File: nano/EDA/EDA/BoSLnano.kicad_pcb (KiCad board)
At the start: 4 copper layers, 69.2 x 15 mm, 60 parts, among them J1 Micro_SD_Card, J2 Conn_01x07, J3 Conn_01x04, J4 SAMD_DBG, J5 nRF_DBG, J6 Conn_01x10, J7 Conn_01x04, J8 Jack-DC, J9 USB_B_Micro, SW1 SPST, U1 MCP1700-3302E_SOT23, U2 ATSAMD21G18A-MUT, U3 NT3H2111W0FTT, U4 NRF9160, U5 BGA524N6, U6 MSQA6V1W5T2G, U7 MAX40203ANS, U8 MAX40203ANS, Y1 32.768kHz

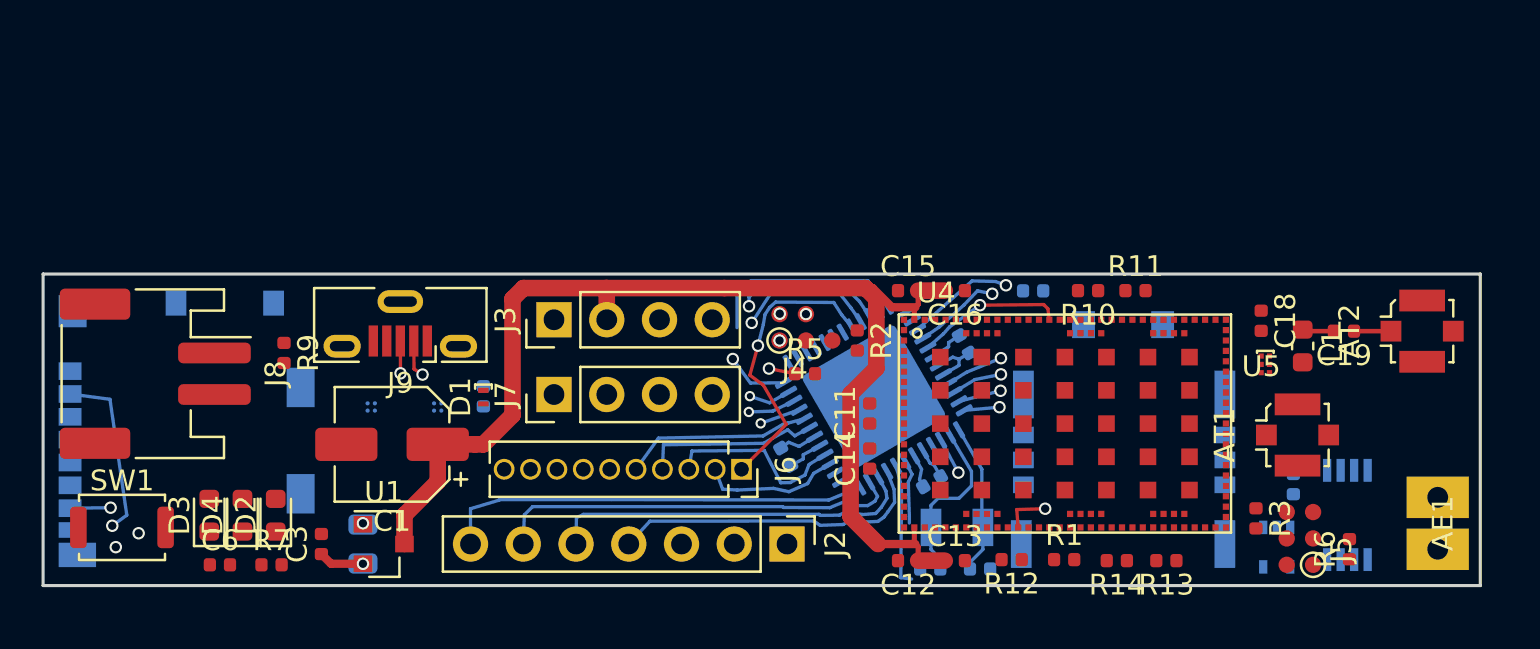
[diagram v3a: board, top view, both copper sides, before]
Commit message: made to be 70 mm
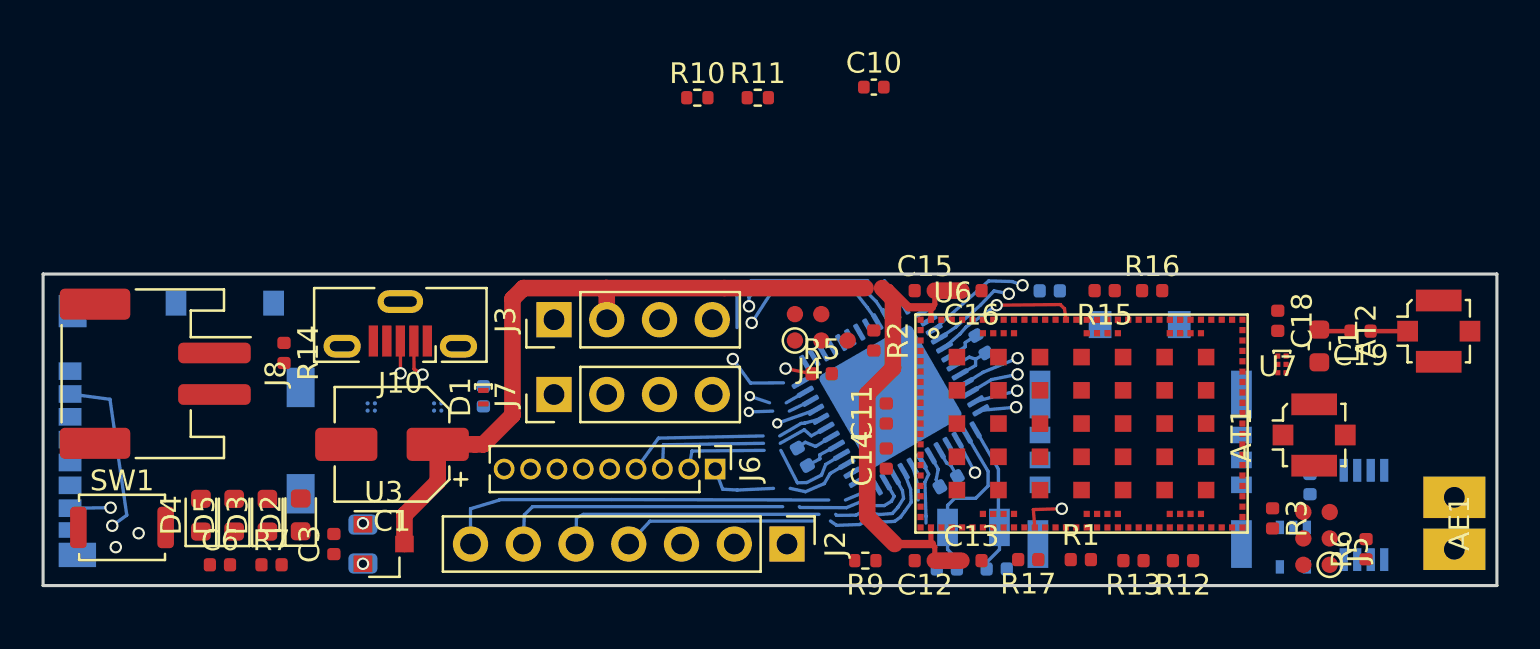
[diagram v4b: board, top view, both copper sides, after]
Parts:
- removed I1: SIM, SIMFootprints:SIMNano
- removed the R14 at (151.7, 113.8)
- removed the U2 at (140.0, 105.9)
- removed the U3 at (162.8, 111.6)
- added C8: 1 μF, Capacitor_SMD:C_0402_1005Metric, B.Cu at (145.2, 103.4)
- added D2: LED, LED_SMD:LED_0603_1608Metric, F.Cu at (112.4, 111.6)
- added J9: SIM, SIMFootprints:SIMNano, B.Cu at (152.8, 114.5)
- added R15: 3.3 kΩ, Resistor_SMD:R_0402_1005Metric, F.Cu at (151.1, 100.8)
- added R16: 3.3 kΩ, Resistor_SMD:R_0402_1005Metric, F.Cu at (153.4, 100.8)
- added R17: 10 kΩ, Resistor_SMD:R_0402_1005Metric, F.Cu at (147.4, 113.8)
- added R9: 3.3 kΩ, Resistor_SMD:R_0402_1005Metric, F.Cu at (139.6, 113.8)
- added U7: BGA524N6, SIMFootprints:TSNP-6-2, F.Cu at (159.4, 104.0)
- added U8: MSQA6V1W5T2G, Package_TO_SOT_SMD:SOT-353_SC-70-5, B.Cu at (160.2, 113.2)
- C10: moved to F.Cu
- C9: value 1 μF -> 100 nF
- J6: value Conn_01x10 -> Conn_01x09; footprint Connector_PinSocket_1.27mm:PinSocket_1x10_P1.27mm_Vertical -> Connector_PinHeader_1.27mm:PinHeader_1x09_P1.27mm_Vertical
- R10: value 3.3 kΩ -> 12 MΩ
- R11: value 3.3 kΩ -> 3.3 MΩ
- R13: value 10 kΩ -> 18 kΩ
- U4: value NRF9160 -> ATSAMD21G18A-MUT; footprint SIMFootprints:nRF9160 -> Package_DFN_QFN:QFN-48-1EP_7x7mm_P0.5mm_EP5.15x5.15mm; moved to B.Cu
- U5: value BGA524N6 -> NT3H2111W0FTT; footprint SIMFootprints:TSNP-6-2 -> Package_SO:TSSOP-8_3x3mm_P0.65mm; moved to B.Cu
- U6: value MSQA6V1W5T2G -> NRF9160; footprint Package_TO_SOT_SMD:SOT-353_SC-70-5 -> SIMFootprints:nRF9160; moved to F.Cu
- moved R10 21.0 mm to (131.5, 91.5), turned to 0 degrees
- moved R11 20.4 mm to (134.4, 91.5)
- moved C10 19.2 mm to (140.0, 91.0), turned to 0 degrees
- moved U6 11.1 mm to (150.0, 107.2), turned to 0 degrees
- moved U5 9.11 mm to (163.6, 111.6), turned to 90 degrees
- moved U4 8.50 mm to (140.8, 105.9), turned to 120 degrees
- moved R12 8.25 mm to (154.9, 113.8)
- moved C9 6.66 mm to (143.6, 110.0), turned to 210 degrees
- moved R13 1.59 mm to (152.5, 113.8)
- moved J6 1.27 mm to (132.4, 109.4)
- moved C17 0.80 mm to (148.5, 100.8)
- moved C19 0.80 mm to (163.4, 102.8)
- moved C7 0.80 mm to (136.6, 108.8)
- moved J5 0.80 mm to (161.3, 115.3)
- moved R1 0.80 mm to (150.0, 113.8)
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- renumbered D2 to D3, D3 to D4, D4 to D5, J9 to J10, R9 to R14, U7 to U1, U8 to U2, U1 to U3
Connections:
- C10 pad 1: -BATT -> Net-(C10-Pad1)
- C10 pad 2: V_3.3 -> -BATT
- C9 pad 1: V_3.3 -> -BATT
- C9 pad 2: -BATT -> V_3.3
- D4 pad 2: Net-(D3-Pad2) (its old number) -> Net-(D4-Pad2)
- D5 pad 2: Net-(D4-Pad2) -> Net-(D5-Pad2)
- J6 pad 1: D1 -> D2
- J6 pad 2: D2 -> D3
- J6 pad 3: D3 -> D4
- J6 pad 4: D4 -> D5
- J6 pad 5: D5 -> D6
- J6 pad 6: D6 -> D7
- J6 pad 7: D7 -> D8
- J6 pad 8: D8 -> D9
- J6 pad 9: D9 -> D10
- R10 pad 1: nRF_STAT -> Net-(C10-Pad1)
- R10 pad 2: Net-(D3-Pad2) (its old number) -> -BATT
- R11 pad 1: nRF_PWR -> Net-(C10-Pad1)
- R11 pad 2: Net-(D4-Pad2) -> +BATT
- R12 pad 1: nRF_RST -> USB_V
- R12 pad 2: V_3.3 -> Net-(R12-Pad2)
- R13 pad 1: USB_V -> Net-(R12-Pad2)
- R13 pad 2: Net-(R13-Pad2) -> -BATT
- U4 pad 1: -BATT -> Net-(C4-Pad1)
- U4 pad 10: Net-(U4-Pad10) -> A4
- U4 pad 11: -BATT -> A5
- U4 pad 12: V_3.3 -> A6
- U4 pad 13: Net-(C14-Pad2) -> SDA
- U4 pad 14: -BATT -> SCL
- U4 pad 15: Net-(U4-Pad15) -> D2
- U4 pad 16: Net-(U4-Pad16) -> D3
- U4 pad 17: -BATT -> V_3.3
- U4 pad 18: RX -> -BATT
- U4 pad 19: TX -> D4
- U4 pad 2: Net-(U4-Pad2) -> Net-(C5-Pad2)
- U4 pad 20: Net-(U4-Pad20) -> D5
- U4 pad 21: -BATT -> SD_MOSI
- U4 pad 22: VPP -> SD_SCLK
- U4 pad 23: Net-(U4-Pad23) -> SD_CS
- U4 pad 24: Net-(U4-Pad24) -> SD_MISO
- U4 pad 25: Net-(U4-Pad25) -> D8
- U4 pad 26: Net-(U4-Pad26) -> D9
- U4 pad 27: -BATT -> Net-(D1-Pad2)
- U4 pad 28: Net-(U4-Pad28) -> D10
- U4 pad 29: Net-(U4-Pad29) -> D6
- U4 pad 3: Net-(U4-Pad3) -> A0
- U4 pad 30: Net-(U4-Pad30) -> D7
- U4 pad 31: -BATT -> NFC_I
- U4 pad 32: nRF_RST -> nRF_EN
- U4 pad 33: nRF_SWCLK -> USB_DM
- U4 pad 34: nRF_SWDIO -> USB_DP
- U4 pad 35: Net-(U4-Pad35) -> -BATT
- U4 pad 36: -BATT -> V_3.3
- U4 pad 37: Net-(U4-Pad37) -> TX
- U4 pad 38: Net-(U4-Pad38) -> RX
- U4 pad 39: Net-(U4-Pad39) -> nRF_RST
- U4 pad 4: Net-(U4-Pad4) -> VNFC
- U4 pad 40: Net-(U4-Pad40) -> RST
- U4 pad 41: -BATT -> nRF_SW_EN
- U4 pad 42: Net-(R13-Pad2) -> -BATT
- U4 pad 43: Net-(I1-Pad2) -> V_3.3
- U4 pad 44: -BATT -> V_3.3
- U4 pad 45: Net-(U4-Pad45) -> SWCLK
- U4 pad 46: Net-(I1-Pad3) -> SWDIO
- U4 pad 47: -BATT -> A1
- U4 pad 48: Net-(I1-Pad6) -> A2
- U4 pad 49: Net-(C17-Pad2) -> (no net)
- U4 pad 6: -BATT -> V_3.3
- U4 pad 7: -BATT -> Net-(R9-Pad1)
- U4 pad 8: -BATT -> Net-(C10-Pad1)
- U4 pad 9: -BATT -> A3
- U5 pad 1: -BATT -> Net-(AE1-Pad2)
- U5 pad 2: V_3.3 -> -BATT
- U5 pad 3: Net-(U4-Pad67) -> SCL
- U5 pad 4: -BATT -> NFC_I
- U5 pad 5: Net-(L1-Pad2) -> SDA
- U5 pad 6: Net-(U4-Pad93) -> VNFC
- U6 pad 1: Net-(I1-Pad2) -> -BATT
- U6 pad 2: -BATT -> Net-(U6-Pad2)
- U6 pad 3: Net-(I1-Pad3) -> Net-(U6-Pad3)
- U6 pad 4: Net-(I1-Pad6) -> Net-(U6-Pad4)
- U6 pad 5: Net-(C17-Pad2) -> -BATT
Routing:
- net D1: track 14.1 -> 0.00 mm, vias 1 -> 0
- net nRF_EN: track 5.93 -> 0.00 mm
- net VNFC: track 3.11 -> 0.00 mm
- net Net-(R9-Pad1): track 0.00 -> 3.11 mm
- net V_3.3: track 18.5 -> 16.3 mm, vias 2 -> 1
- net Net-(C10-Pad1): track 0.00 -> 1.66 mm
- net SWCLK: vias 2 -> 1
- net SWDIO: vias 2 -> 1
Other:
- board size 69.2 x 15 mm -> 70 x 15 mm
- board text added: "BoSLnano rev 0.1.0"

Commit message: began routing nano
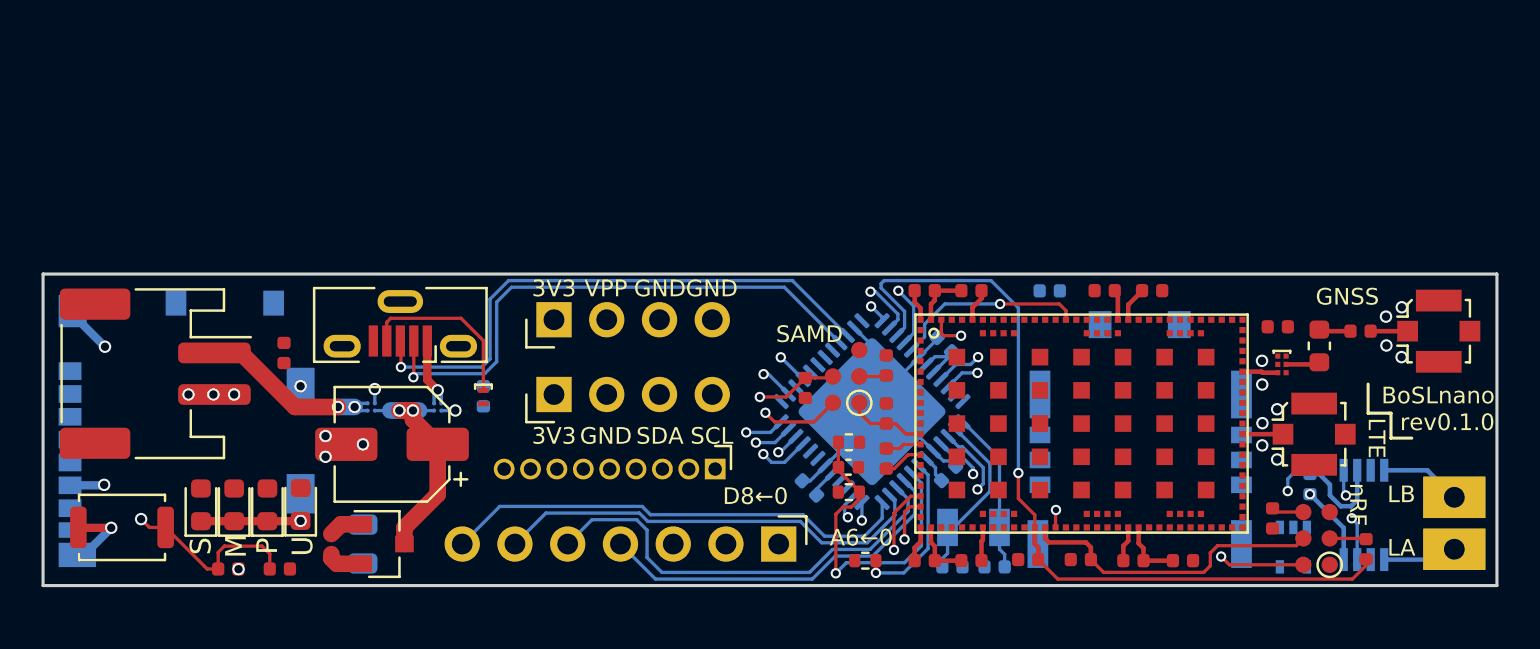
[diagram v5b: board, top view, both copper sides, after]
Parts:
- moved R11 19.5 mm to (138.8, 110.5), turned to 180 degrees
- moved C10 18.3 mm to (138.8, 109.3)
- moved R10 18.1 mm to (138.8, 108.1)
- moved J4 6.17 mm to (138.7, 107.5), turned to 90 degrees
- moved R2 4.01 mm to (136.7, 105.5), turned to 90 degrees
- moved R5 3.14 mm to (140.6, 104.4), turned to 270 degrees
- moved C8 1.76 mm to (143.4, 103.4), turned to 135 degrees
- moved C7 1.54 mm to (136.9, 110.3), turned to 135 degrees
- moved U4 1.15 mm to (139.9, 106.6), turned to 135 degrees
- moved D2 0.50 mm to (112.4, 111.1)
- moved D3 0.50 mm to (110.8, 111.1)
- moved D4 0.50 mm to (107.6, 111.1)
- moved D5 0.50 mm to (109.2, 111.1)
- moved C6 0.45 mm to (108.9, 114.2)
- moved R7 0.45 mm to (111.4, 114.2)
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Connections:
- J6 pad 1: D2 -> D0
- J6 pad 2: D3 -> D1
- J6 pad 3: D4 -> D2
- J6 pad 4: D5 -> D3
- J6 pad 5: D6 -> D4
- J6 pad 6: D7 -> D5
- J6 pad 7: D8 -> D6
- J6 pad 8: D9 -> D7
- J6 pad 9: D10 -> D8
- U4 pad 26: D9 -> NFC_I
- U4 pad 28: D10 -> nRF_EN
- U4 pad 31: NFC_I -> D0
- U4 pad 32: nRF_EN -> D1
- U4 pad 49: (no net) -> -BATT
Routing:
- net SD_CS: track 44.2 -> 1.84 mm, vias 2 -> 1
- net RST: track 16.9 -> 58.7 mm
- net -BATT: track 5.14 -> 46.3 mm, vias 1 -> 24
- net VPP: track 57.9 -> 16.8 mm, vias 0 -> 2
- net NFC_I: track 0.00 -> 35.2 mm, vias 0 -> 2
- net SD_MISO: track 37.0 -> 1.90 mm, vias 2 -> 1
- net SD_MOSI: track 34.2 -> 2.46 mm, vias 2 -> 1
- net SD_SCLK: track 32.6 -> 1.17 mm, vias 2 -> 1
- net SCL: track 0.00 -> 30.2 mm, vias 0 -> 2
- net SDA: track 0.00 -> 28.1 mm, vias 0 -> 2
- net RX: track 0.00 -> 26.3 mm, vias 0 -> 2
- net VNFC: track 0.00 -> 24.3 mm, vias 0 -> 2
- net TX: track 0.00 -> 22.3 mm, vias 0 -> 2
- net nRF_RST: track 18.3 -> 39.6 mm, vias 2 -> 1
- net A2: track 19.2 -> 0.00 mm, vias 1 -> 0
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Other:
- board text added: "3V3"
- board text added: "A6←0"
- board text added: "BoSLnano rev0.1.0"
- board text added: "D8←0"
- board text added: "GND"
- board text added: "GNSS"
- board text added: "LB LA"
- board text added: "LTE"
- board text added: "M"
- board text added: "P"
- board text added: "S"
- board text added: "SAMD"
- board text added: "SCL"
- board text added: "SDA"
- board text added: "U"
- board text added: "VPP"
- board text added: "nRF"

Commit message: finished PCB layout
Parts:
- R12, R9: moved to B.Cu
- moved R12 36.7 mm to (118.3, 110.3), turned to 0 degrees
- moved R9 25.1 mm to (114.8, 110.3)
- moved J2 15.2 mm to (120.2, 113.0), turned to 90 degrees
- moved R14 4.20 mm to (111.6, 108.0)
- moved C17 0.63 mm to (147.8, 100.8), turned to 180 degrees
- moved R17 0.38 mm to (147.8, 113.8), turned to 0 degrees
- moved C15 0.37 mm to (142.4, 101.2)
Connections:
- J10 pad 6: Net-(J10-Pad6) -> (no net)
- J2 pad 1: A0 -> A6
- J2 pad 2: A1 -> A5
- J2 pad 3: A2 -> A4
- J2 pad 5: A4 -> A2
- J2 pad 6: A5 -> A1
- J2 pad 7: A6 -> A0
- U4 pad 10: A4 -> A5
- U4 pad 11: A5 -> A6
- U4 pad 12: A6 -> Net-(C10-Pad1)
- U4 pad 15: D2 -> D5
- U4 pad 16: D3 -> D4
- U4 pad 19: D4 -> D3
- U4 pad 20: D5 -> D2
- U4 pad 25: D8 -> D0
- U4 pad 26: NFC_I -> D1
- U4 pad 28: nRF_EN -> D6
- U4 pad 29: D6 -> D7
- U4 pad 30: D7 -> D8
- U4 pad 31: D0 -> NFC_I
- U4 pad 32: D1 -> nRF_EN
- U4 pad 47: A1 -> A2
- U4 pad 48: A2 -> A1
- U4 pad 8: Net-(C10-Pad1) -> A4
- U8 pad 1: Net-(J9-Pad2) -> Net-(J9-Pad6)
- U8 pad 4: Net-(J9-Pad6) -> Net-(J9-Pad2)
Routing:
- net -BATT: track 46.3 -> 255.8 mm, vias 24 -> 55
- net V_3.3: track 11.3 -> 133.0 mm, vias 0 -> 9
- net SD_CS: track 1.84 -> 69.4 mm, vias 1 -> 2
- net VPP: track 16.8 -> 77.1 mm
- net Net-(D5-Pad2): track 0.00 -> 54.4 mm, vias 0 -> 2
- net Net-(D4-Pad2): track 0.00 -> 50.4 mm, vias 0 -> 2
- net SD_MOSI: track 2.46 -> 41.4 mm, vias 1 -> 2
- net Net-(R12-Pad2): track 3.11 -> 41.6 mm, vias 0 -> 3
- net SD_SCLK: track 1.17 -> 38.9 mm, vias 1 -> 2
- net SD_MISO: track 1.90 -> 37.1 mm, vias 1 -> 2
- net +BATT: track 9.22 -> 38.6 mm, vias 2 -> 5
- net Net-(R9-Pad1): track 7.76 -> 35.2 mm, vias 1 -> 2
- net Net-(C17-Pad2): track 0.00 -> 26.5 mm, vias 0 -> 1
- net A2: track 0.00 -> 25.3 mm, vias 0 -> 1
- net nRF_EN: track 12.3 -> 36.3 mm, vias 2 -> 4
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- added copper zone on F.Cu, net -BATT
- added copper zone on In2.Cu, net V_3.3
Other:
- outline, holes or cut-outs redrawn
